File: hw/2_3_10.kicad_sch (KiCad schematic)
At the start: 15 parts, among them M2 Motor_Servo, M3 Motor_Servo, M4 Motor_Servo, M5 Motor_Servo, M6 Motor_Servo, M7 Motor_Servo, U7 MC7905, U8 ATmega2560-16A

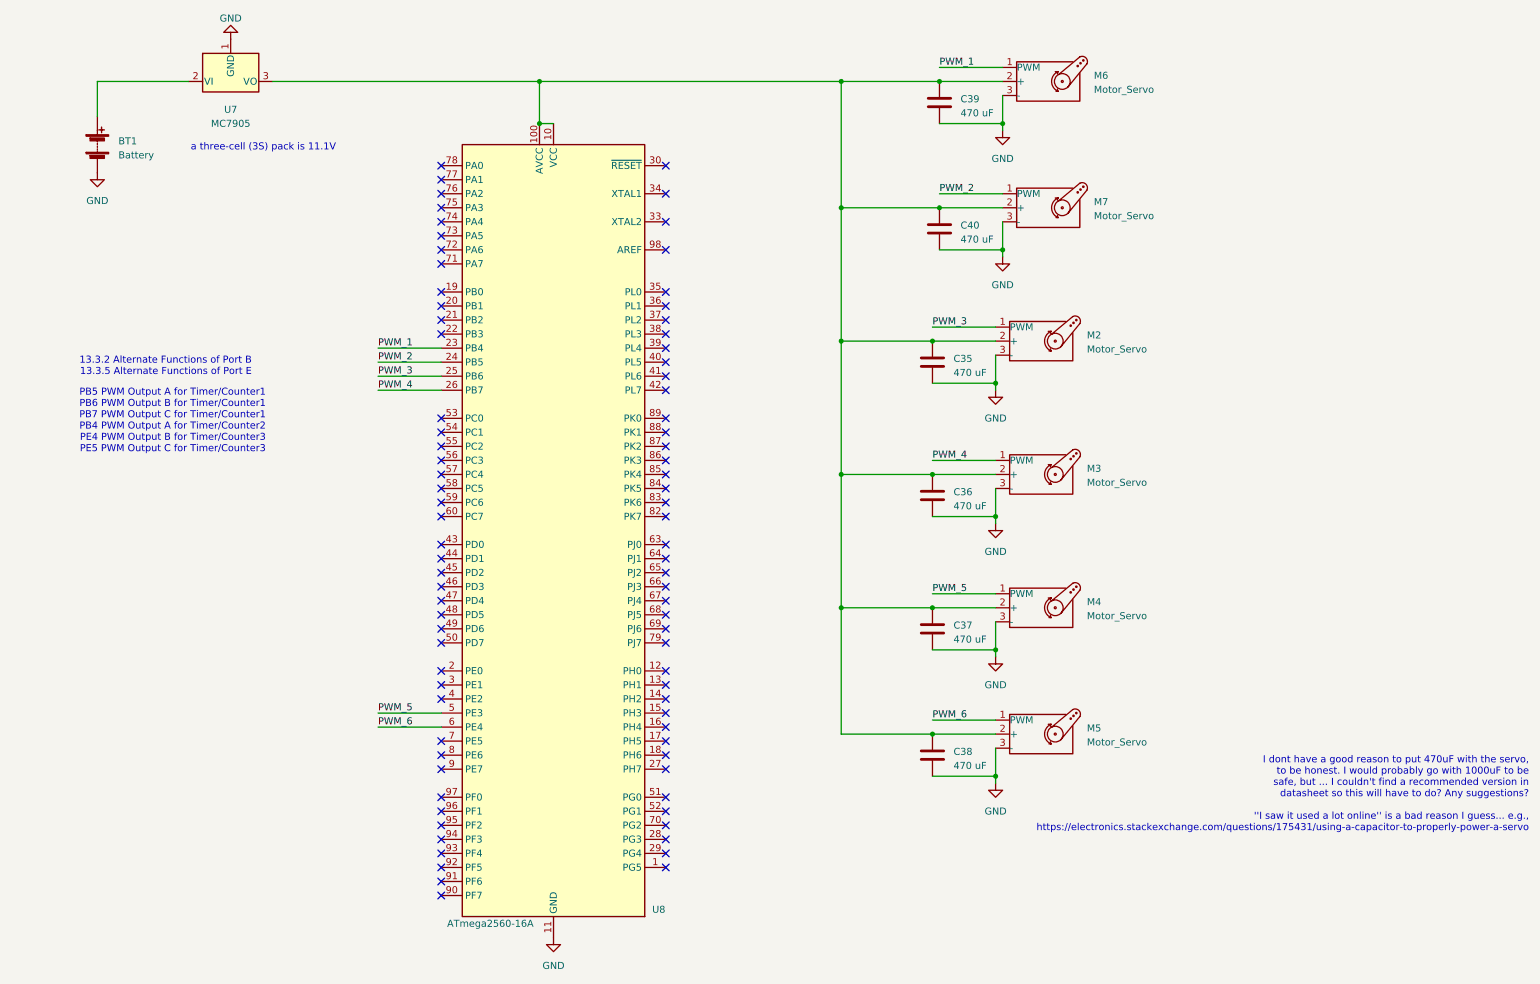
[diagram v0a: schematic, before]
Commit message: Add LM2576S-5 to 2.3.10
Signed-off-by: ckalina <46683072+ckalina@users.noreply.github.com>
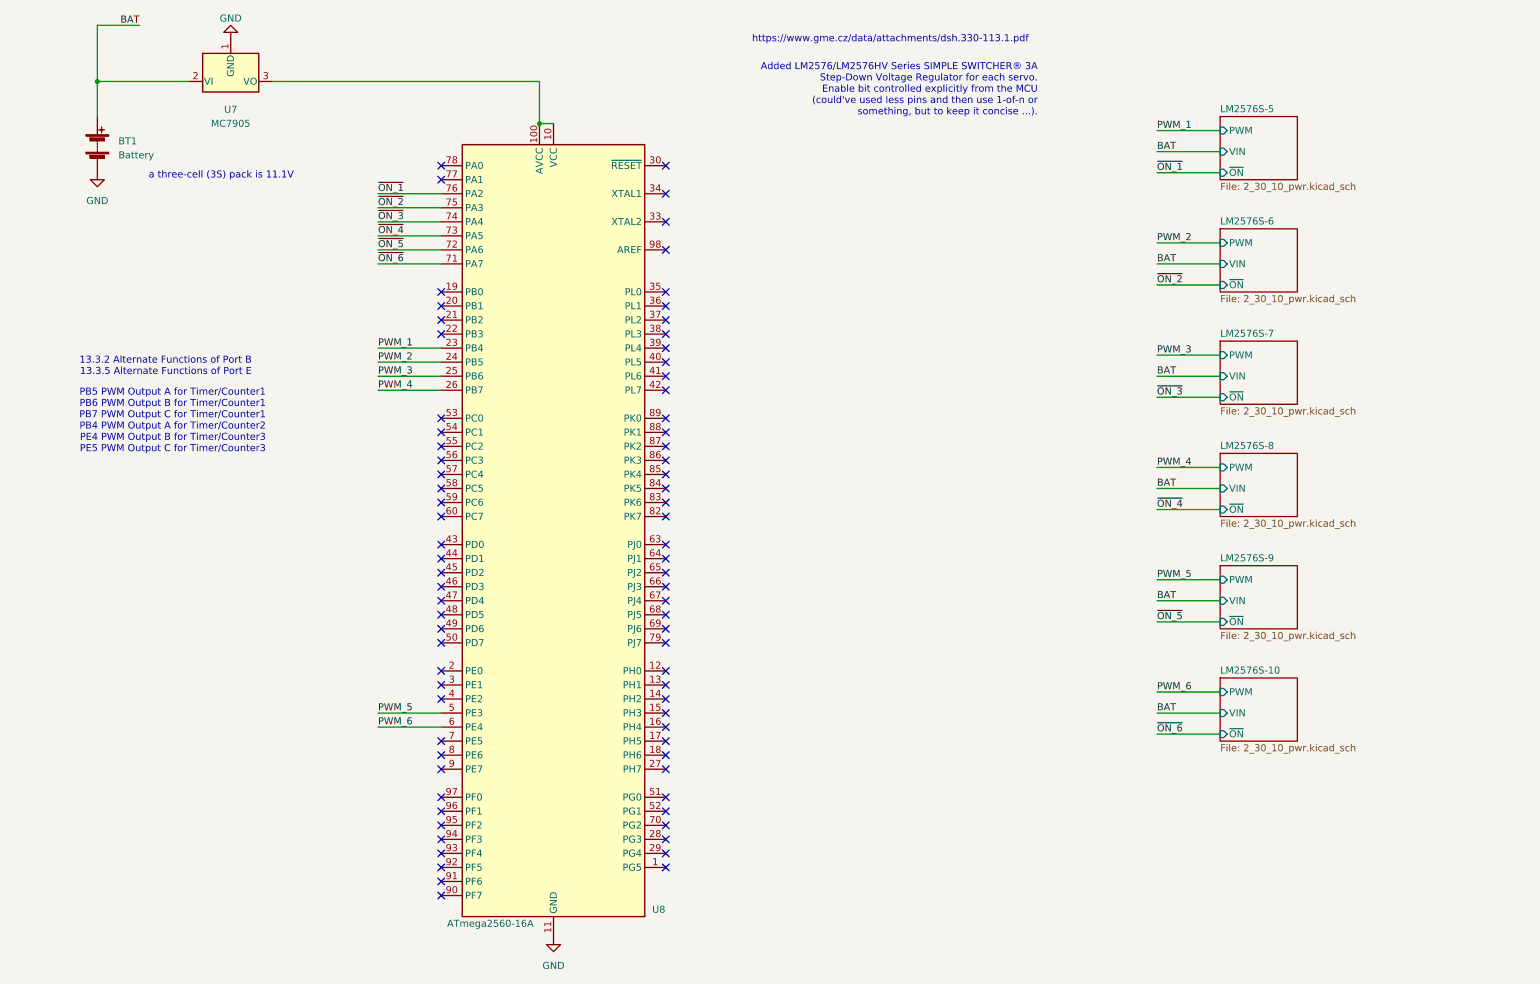
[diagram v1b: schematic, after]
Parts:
- removed C35, C36, C37, C38, C39, C40: 470 uF, symbol Device:C
- removed M2, M3, M4, M5, M6, M7: Motor_Servo, symbol Motor:Motor_Servo
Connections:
- net BAT: now reaches BT1.1 (+), U7.2 (VI)
- net ~ON_6: now reaches U8.71 (PA7)
- net ~ON_5: now reaches U8.72 (PA6)
- net ~ON_4: now reaches U8.73 (PA5)
- net ~ON_3: now reaches U8.74 (PA4)
- net ~ON_2: now reaches U8.75 (PA3)
- net ~ON_1: now reaches U8.76 (PA2)
- no-connect marks 84 -> 78
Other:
- added sheet LM2576S-10 (2_30_10_pwr.kicad_sch)
- added sheet LM2576S-5 (2_30_10_pwr.kicad_sch)
- added sheet LM2576S-6 (2_30_10_pwr.kicad_sch)
- added sheet LM2576S-7 (2_30_10_pwr.kicad_sch)
- added sheet LM2576S-8 (2_30_10_pwr.kicad_sch)
- added sheet LM2576S-9 (2_30_10_pwr.kicad_sch)
- note added: "Added LM2576/LM2576HV Series SIMPLE SWITCHER® 3A Step-Down Voltage Regulator for each servo. Enable bit controlled explicitly from the MCU (could've used less pins and then use 1-of-n or something, but to keep it concise ...)."
- note added: "https://www.gme.cz/data/attachments/dsh.330-113.1.pdf"
- note removed: "I dont have a good reason to put 470uF with the servo, to be honest. I would probably go with 1000uF to be safe, but ... I couldn't find a recommended version in datasheet so this will have to do? Any suggestions? ''I saw it used a lot online'' is a bad reason I guess... e.g., https://electronics.stackexchange.com/questions/175431/using-a-capacitor-to-properly-power-a-servo"
